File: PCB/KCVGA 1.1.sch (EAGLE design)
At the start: 49 parts, among them IC1 M68AW128MND, IC2 74245ADB, IC3 74245ADB, IC4 LD117AS12TR, IC5 LD117AS33TR, U1 XC3S50ATQ144, U2 PIC32MX250F128B_I_SS, X1 D-SUB15, X2 MINI-USB

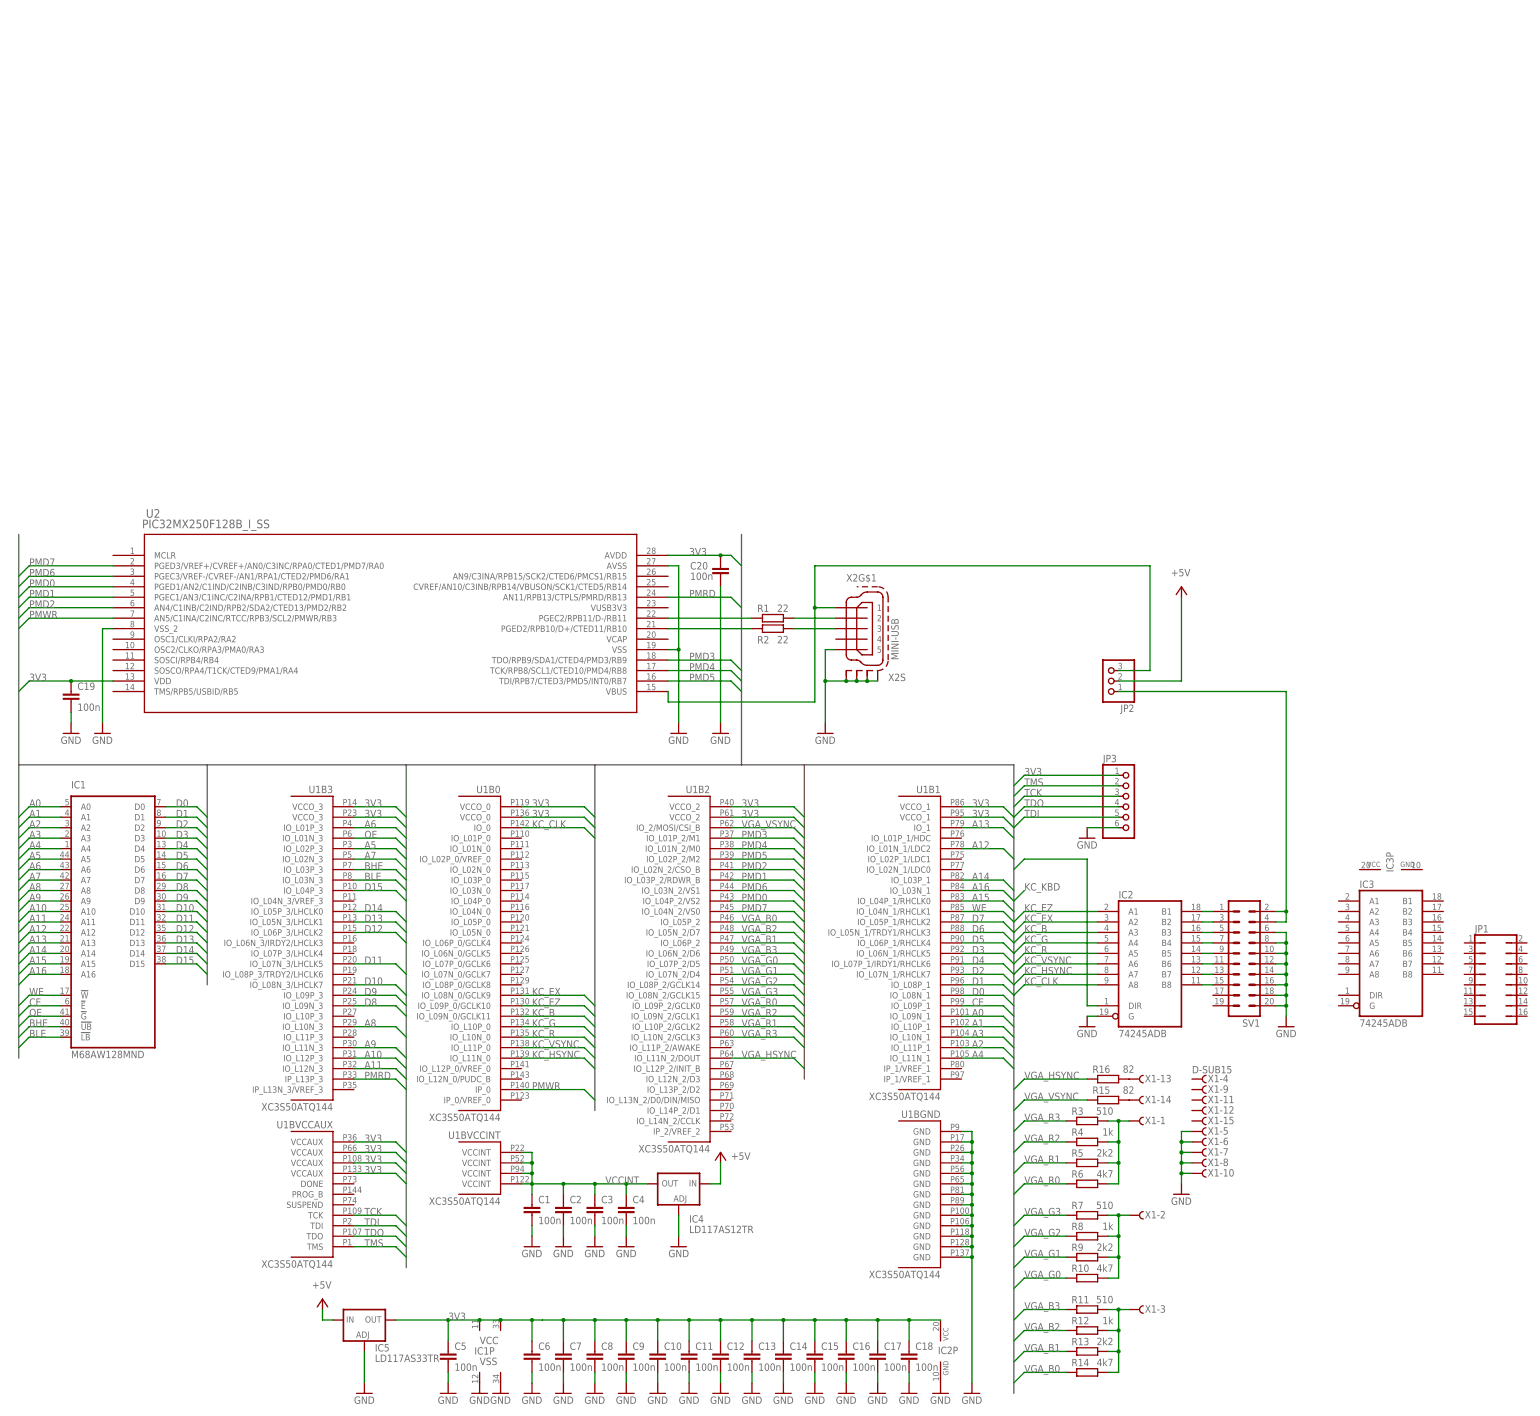
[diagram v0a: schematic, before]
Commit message: Added crystal oscillator, voltage regulators, FPGA config lines
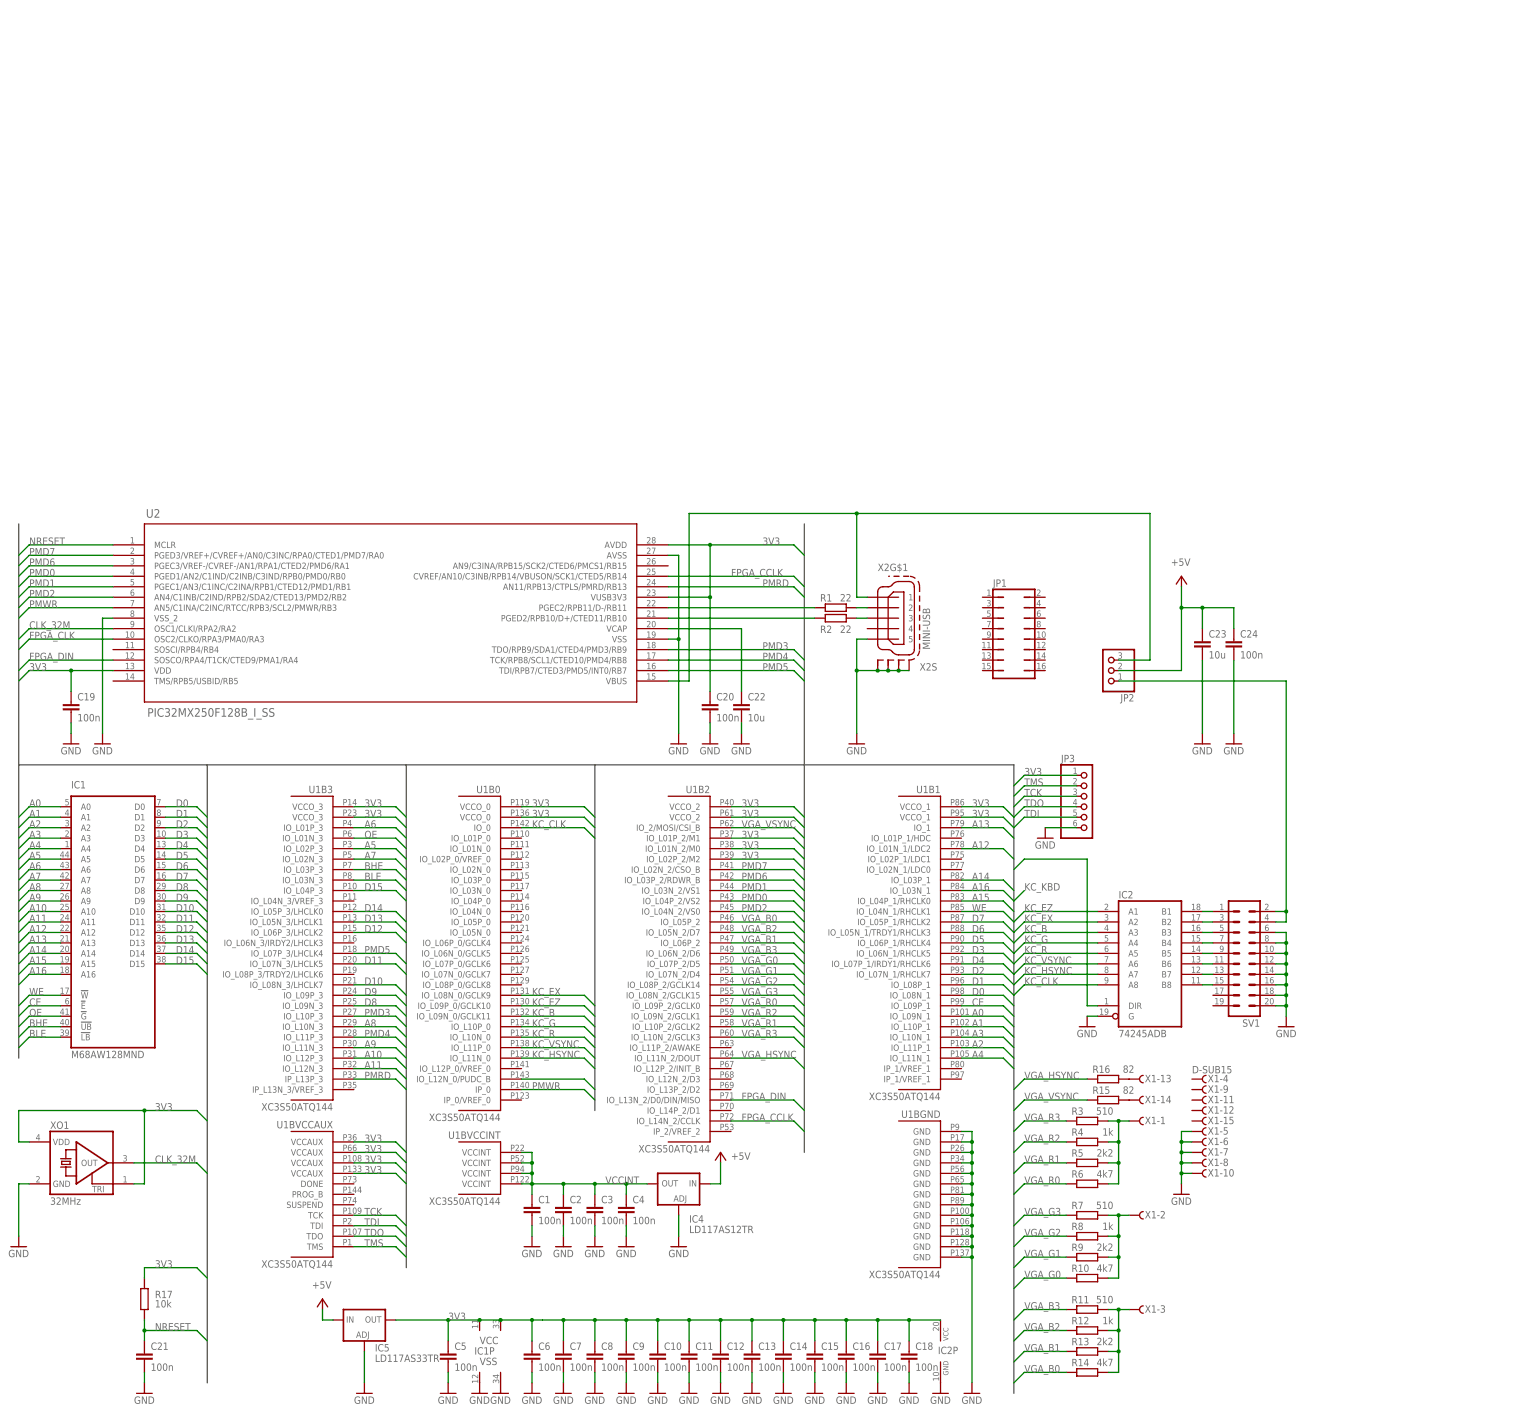
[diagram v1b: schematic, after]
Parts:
- removed IC3: 74245ADB, 74xx-eu:74245ADB
- added C21, C24: 100n, rcl:C-EUC0603K
- added C22, C23: 10u, rcl:C-EUC1206K
- added R17: 10k, rcl:R-EU_R0603
- added XO1: 32MHz, crystal:ASE
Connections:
- new net CLK_32M: U2.OSC1/CLKI/RPA2/RA2, XO1.OUT
- new net FPGA_CCLK: U1B2.IO_L14N_2/CCLK, U2.CVREF/AN10/C3INB/RPB14/VBUSON/SCK1/CTED5/RB14
- new net FPGA_CLK: U2.OSC2/CLKO/RPA3/PMA0/RA3
- new net FPGA_DIN: U1B2.IO_L13N_2/D0/DIN/MISO, U2.SOSCO/RPA4/T1CK/CTED9/PMA1/RA4
- new net N$16: C22.1, U2.VCAP
- new net NRESET: C21.1, R17.1, U2.MCLR
- net +5V: now also C23.1, C24.1
- net 3V3: now also R17.2, U1B0.IO_L12N_0/PUDC_B, U1B2.IO_L01N_2/M0, U1B2.IO_L01P_2/M1, U1B2.IO_L02P_2/M2, U2.VUSB3V3, XO1.TRI, XO1.VDD
- net GND: now also C21.2, C22.2, C23.2, C24.2, XO1.GND
- net PMD1: now also U1B2.IO_L03N_2/VS1; no longer U1B2.IO_L03P_2/RDWR_B
- net PMD2: now also U1B2.IO_L04N_2/VS0; no longer U1B2.IO_L02N_2/CSO_B
- net PMD3: now also U1B3.IO_L10P_3; no longer U1B2.IO_L01P_2/M1
- net PMD4: now also U1B3.IO_L11P_3; no longer U1B2.IO_L01N_2/M0
- net PMD5: now also U1B3.IO_L07P_3/LHCLK4; no longer U1B2.IO_L02P_2/M2
- net PMD6: now also U1B2.IO_L03P_2/RDWR_B; no longer U1B2.IO_L03N_2/VS1
- net PMD7: now also U1B2.IO_L02N_2/CSO_B; no longer U1B2.IO_L04N_2/VS0
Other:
- moved on the sheet: C19, C20, JP1, JP2, JP3, R1, R2, U2, X2G$1, X2S

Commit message: completed FPGA configuration interface, tidied up
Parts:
- added LED1, LED2: (no value), led:LEDCHIPLED_0603
- added R18, R19: 10k, rcl:R-EU_R0603
- added R20, R21: 330, rcl:R-EU_R0603
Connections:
- net BHE renamed !BHE
- net BLE renamed !BLE
- net CE renamed !CE
- net NRESET renamed !RESET
- net OE renamed !OE
- net PMRD renamed !PMRD
- net PMWR renamed !PMWR
- net WE renamed !WE
- new net !INIT_B: R18.1, U1B2.IO_L12P_2/INIT_B, U2.TMS/RPB5/USBID/RB5
- new net !PROG_B: R19.1, U1BVCCAUX.PROG_B, U2.SOSCI/RPB4/RB4
- new net DONE: R20.1, U1BVCCAUX.DONE
- new net N$21: LED2.A, R20.2
- new net N$22: R21.1, U2.AN9/C3INA/RPB15/SCK2/CTED6/PMCS1/RB15
- new net N$23: LED1.A, R21.2
- net 3V3: now also R18.2, R19.2
- net GND: now also LED1.C, LED2.C, U1BVCCAUX.SUSPEND

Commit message: PCB: First implementation complete
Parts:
- JP1: device jumper:JP8Q -> pinhead:PINHD-1X6
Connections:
- new net !FPGA_RESET: U1B3.IO_L08P_3/TRDY2/LHCLK6
- net !RESET: now also JP1.1
- net 3V3: now also JP1.2
- net FPGA_CLK: now also U1B0.IO_L07N_0/GCLK7
- net GND: now also JP1.3
- net PMD0: now also JP1.4
- net PMD1: now also JP1.5
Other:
- note added: "TODO: !FPGA_RESET, FPGA-Jumper"
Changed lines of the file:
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@@
 <part name="C10" library="rcl" deviceset="C-EU" device="C0603K" value="100n"/>
 <part name="GND13" library="supply1" deviceset="GND" device=""/>
-<part name="JP1" library="jumper" deviceset="JP8Q" device=""/>
 <part name="SV1" library="con-ml" deviceset="ML20" device=""/>
 <part name="GND14" library="supply1" deviceset="GND" device=""/>
@@
 <part name="GND40" library="supply1" deviceset="GND" device=""/>
 <part name="GND41" library="supply1" deviceset="GND" device=""/>
+<part name="JP1" library="pinhead" deviceset="PINHD-1X6" device=""/>
 </parts>
 <sheets>
 <sheet>
 <plain>
+<text x="-58.42" y="172.72" size="6.4516" layer="97">TODO: !FPGA_RESET, FPGA-Jumper</text>
 </plain>
 <instances>
@@
 <instance part="C10" gate="G$1" x="73.66" y="-48.26"/>
 <instance part="GND13" gate="1" x="73.66" y="-58.42"/>
-<instance part="JP1" gate="B" x="160.02" y="127" rot="R270"/>
 <instance part="SV1" gate="1" x="215.9" y="45.72" rot="R180"/>
 <instance part="GND14" gate="1" x="226.06" y="30.48"/>
@@
 <instance part="GND40" gate="1" x="-15.24" y="-58.42"/>
 <instance part="GND41" gate="1" x="114.3" y="157.48"/>
+<instance part="JP1" gate="A" x="170.18" y="124.46"/>
 </instances>
 <busses>
-<bus name="BUS:3V3,!WE,!CE,!OE,!BLE,!BHE,A[0..16],D[0..15],KC_CLK,KC_VSYNC,KC_HSYNC,KC_R,KC_G,KC_B,KC_EX,KC_EY,KC_EZ,KC_KBD,VGA_HSYNC,VGA_VSYNC,VGA_R[0..3],VGA_G[0..3],VGA_B[0..3],PMD[0..7],PMA[0..1],!PMRD,!PMWR,TMS,TCK,TDO,TDI,CLK_32M,FPGA_CLK,!RESET,FPGA_CCLK,FPGA_DIN,!INIT_B,!PROG_B,DONE">
+<bus name="BUS:3V3,!WE,!CE,!OE,!BLE,!BHE,A[0..16],D[0..15],KC_CLK,KC_VSYNC,KC_HSYNC,KC_R,KC_G,KC_B,KC_EX,KC_EY,KC_EZ,VGA_HSYNC,VGA_VSYNC,VGA_R[0..3],VGA_G[0..3],VGA_B[0..3],PMD[0..7],PMA[0..1],!PMRD,!PMWR,TMS,TCK,TDO,TDI,CLK_32M,FPGA_CLK,!RESET,FPGA_CCLK,FPGA_DIN,!INIT_B,!PROG_B,DONE,!FPGA_RESET">
 <segment>
 <wire x1="-35.56" y1="-55.88" x2="-35.56" y2="93.98" width="0.762" layer="92"/>
@@
 <wire x1="-15.24" y1="-50.8" x2="-15.24" y2="-55.88" width="0.1524" layer="91"/>
 </segment>
+<segment>
+<pinref part="JP1" gate="A" pin="3"/>
+<wire x1="167.64" y1="127" x2="149.86" y2="127" width="0.1524" layer="91"/>
+<label x="149.86" y="127" size="1.778" layer="95"/>
+</segment>
 </net>
 <net name="VCCINT" class="0">
@@
 <wire x1="55.88" y1="17.78" x2="40.64" y2="17.78" width="0.1524" layer="91"/>
 </segment>
+<segment>
+<pinref part="JP1" gate="A" pin="2"/>
+<wire x1="167.64" y1="129.54" x2="149.86" y2="129.54" width="0.1524" layer="91"/>
+<label x="149.86" y="129.54" size="1.778" layer="95"/>
+</segment>
 </net>
 <net name="KC_CLK" class="0">
@@
 <label x="93.98" y="60.96" size="1.778" layer="95"/>
 </segment>
+<segment>
+<pinref part="JP1" gate="A" pin="4"/>
+<wire x1="167.64" y1="124.46" x2="149.86" y2="124.46" width="0.1524" layer="91"/>
+<label x="149.86" y="124.46" size="1.778" layer="95"/>
+</segment>
 </net>
 <net name="PMD1" class="0">
@@
 <wire x1="106.68" y1="63.5" x2="91.44" y2="63.5" width="0.1524" layer="91"/>
 <label x="93.98" y="63.5" size="1.778" layer="95"/>
+</segment>
+<segment>
+<pinref part="JP1" gate="A" pin="5"/>
+<wire x1="167.64" y1="121.92" x2="149.86" y2="121.92" width="0.1524" layer="91"/>
+<label x="149.86" y="121.92" size="1.778" layer="95"/>
 </segment>
 </net>
@@
 <label x="-78.74" y="124.46" size="1.778" layer="95"/>
 </segment>
+<segment>
+<pinref part="U1" gate="B0" pin="IO_L07N_0/GCLK7"/>
+<wire x1="58.42" y1="40.64" x2="55.88" y2="43.18" width="0.1524" layer="91"/>
+<wire x1="55.88" y1="43.18" x2="40.64" y2="43.18" width="0.1524" layer="91"/>
+<label x="43.18" y="43.18" size="1.778" layer="95"/>
+</segment>
 </net>
 <net name="!RESET" class="0">
@@
 <label x="-48.26" y="-43.18" size="1.778" layer="95"/>
 </segment>
+<segment>
+<pinref part="JP1" gate="A" pin="1"/>
+<wire x1="167.64" y1="132.08" x2="149.86" y2="132.08" width="0.1524" layer="91"/>
+<label x="149.86" y="132.08" size="1.778" layer="95"/>
+</segment>
 </net>
 <net name="N$16" class="0">
@@
 </segment>
 </net>
+<net name="!FPGA_RESET" class="0">
+<segment>
+<pinref part="U1" gate="B3" pin="IO_L08P_3/TRDY2/LHCLK6"/>
+<wire x1="12.7" y1="40.64" x2="10.16" y2="43.18" width="0.1524" layer="91"/>
+<wire x1="10.16" y1="43.18" x2="0" y2="43.18" width="0.1524" layer="91"/>
+<label x="2.54" y="43.18" size="1.778" layer="95"/>
+</segment>
+</net>

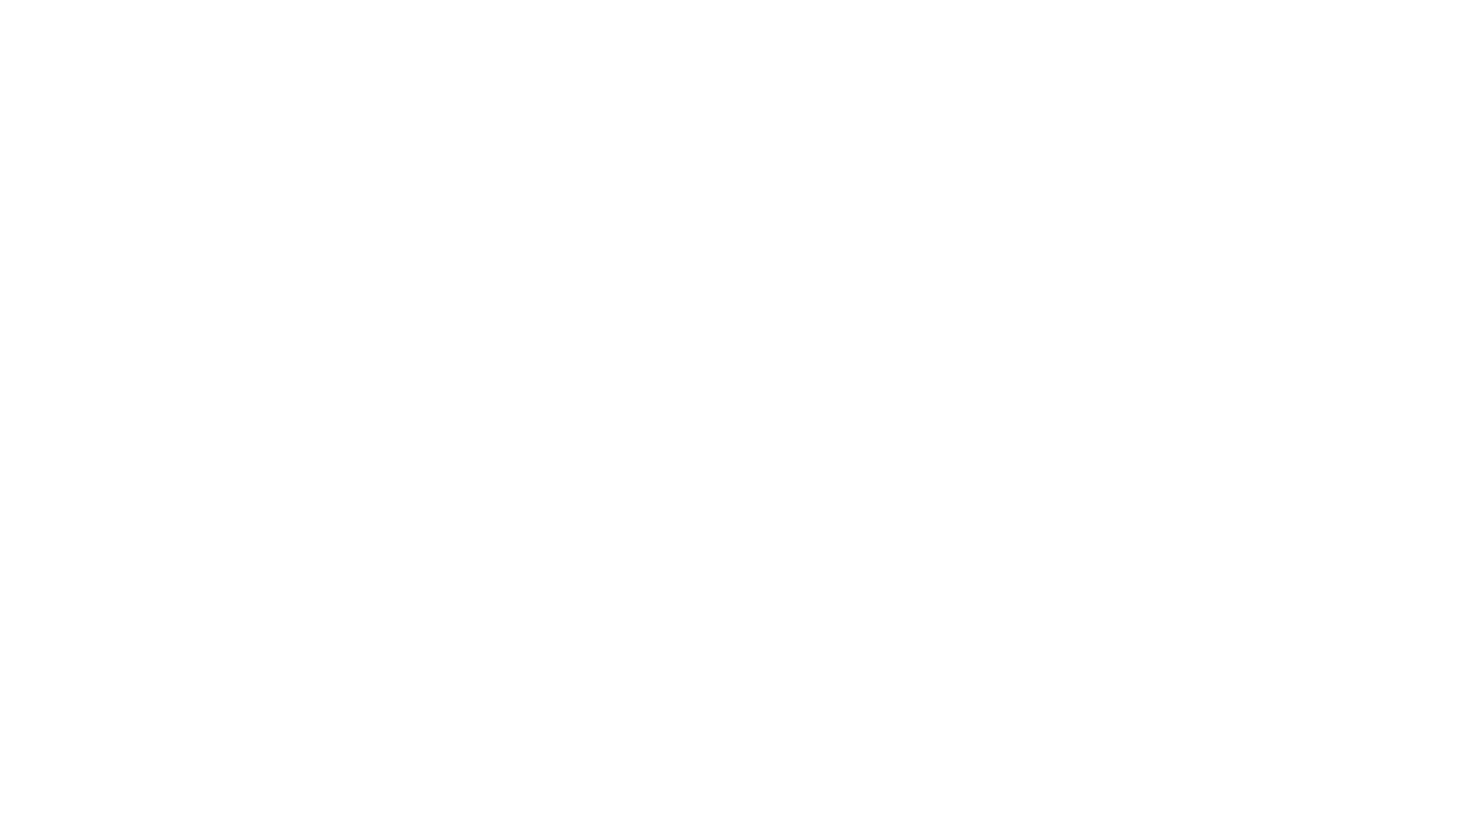
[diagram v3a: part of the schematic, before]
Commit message: Test with PIC32MX270 in TQFP44
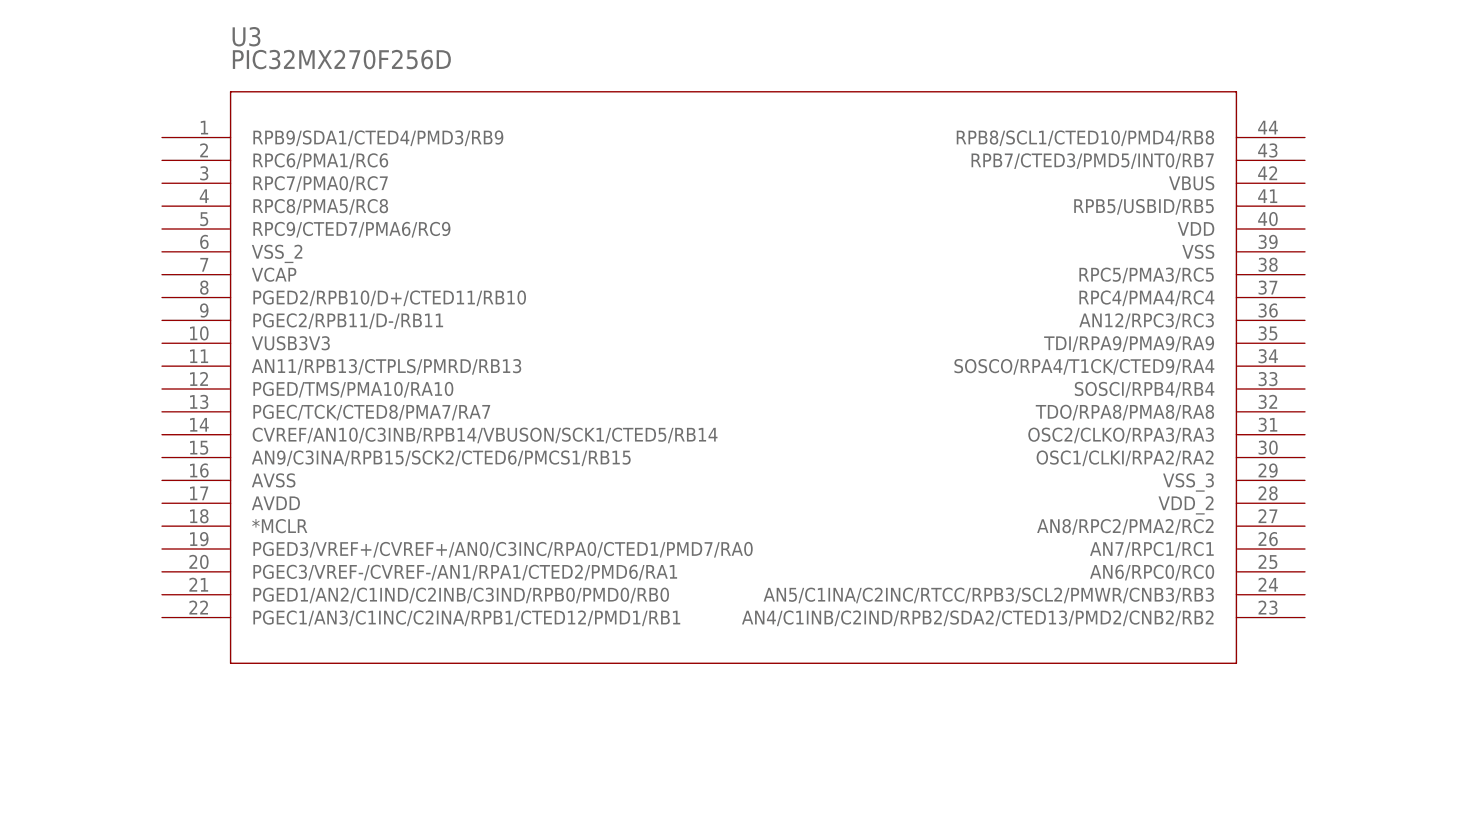
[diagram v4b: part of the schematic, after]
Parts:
- added U3: PIC32MX270F256D, PIC32MX270:PIC32MX250F128D-I_PT
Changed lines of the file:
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@@
 <part name="GND41" library="supply1" deviceset="GND" device=""/>
 <part name="JP1" library="pinhead" deviceset="PINHD-1X6" device=""/>
+<part name="U3" library="PIC32MX270" deviceset="PIC32MX250F128D-I_PT" device="" value="PIC32MX270F256D"/>
 </parts>
 <sheets>
@@
 <instance part="GND41" gate="1" x="114.3" y="157.48"/>
 <instance part="JP1" gate="A" x="170.18" y="124.46"/>
+<instance part="U3" gate="A" x="-55.88" y="264.16"/>
 </instances>
 <busses>
